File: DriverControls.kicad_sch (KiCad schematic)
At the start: 0 parts

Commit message: idk
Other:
- sheet LeaderSOM2 ports: added none; removed +12V_CarCAN, GND_CarCAN

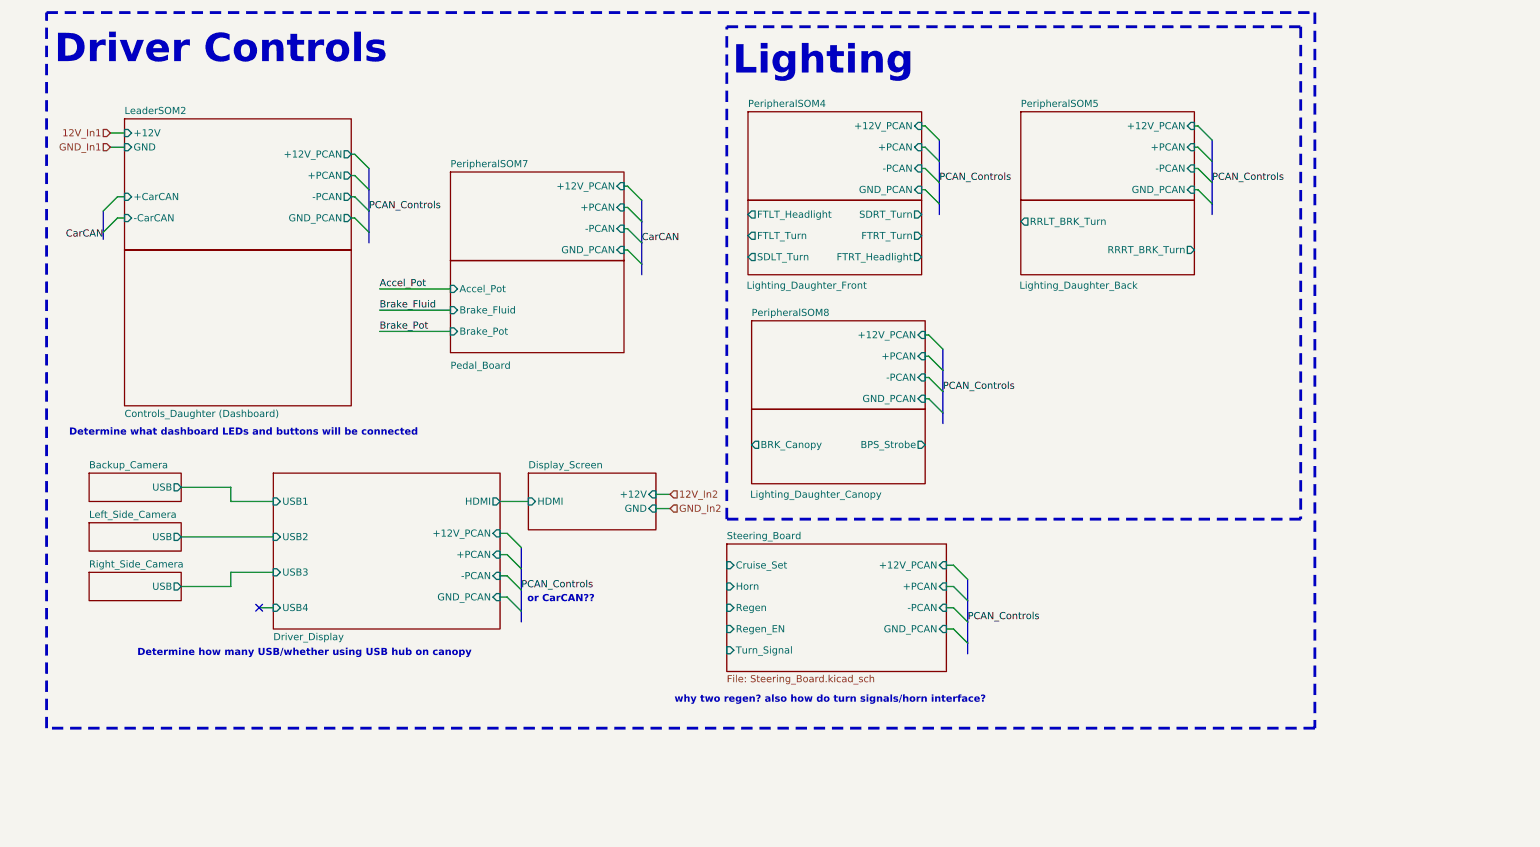
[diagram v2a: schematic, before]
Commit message: Updated Controls + Telemetry
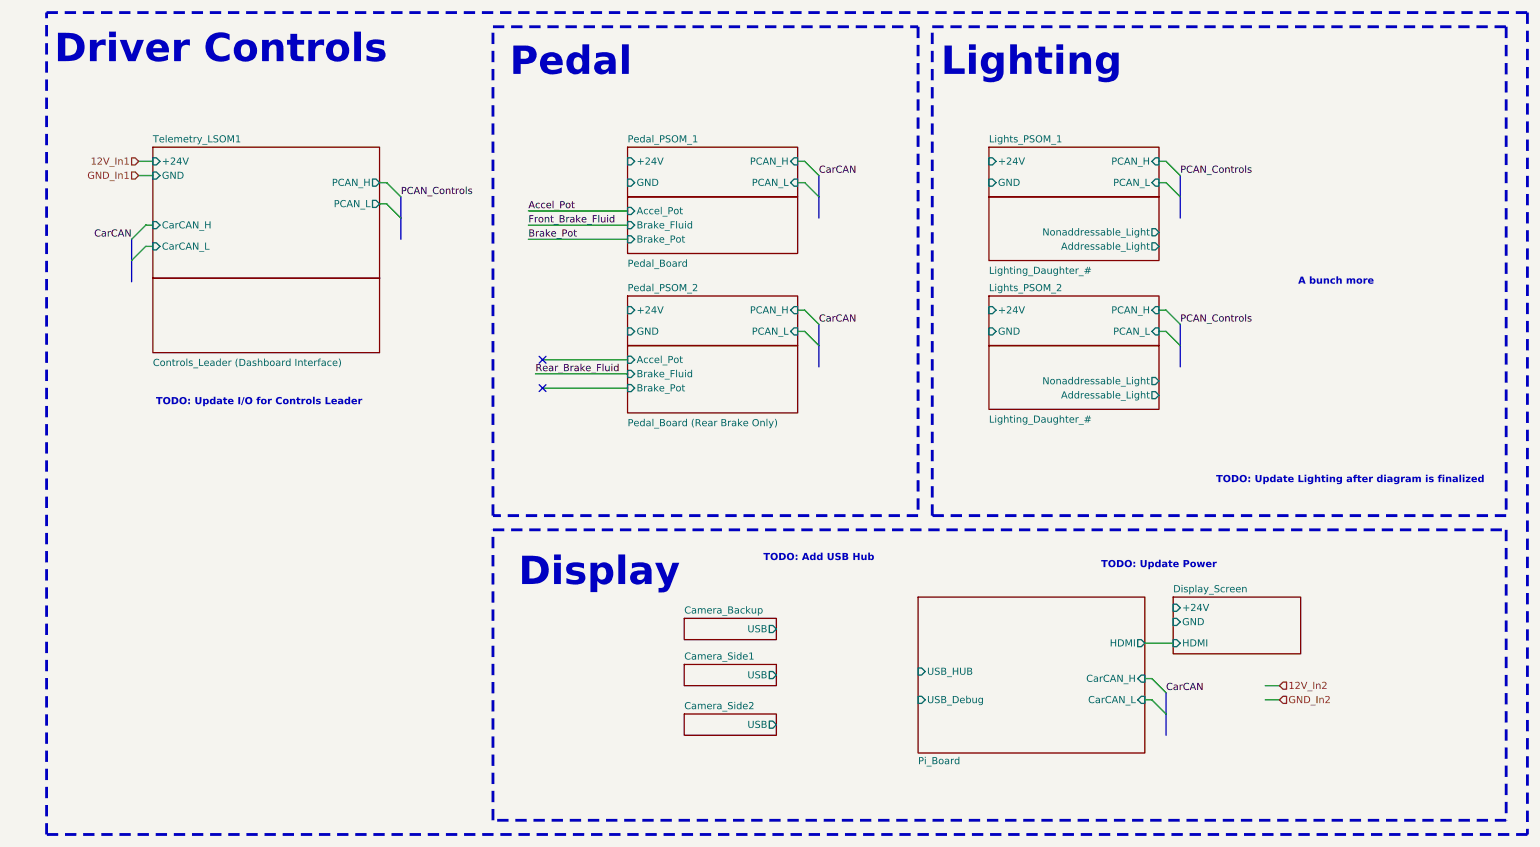
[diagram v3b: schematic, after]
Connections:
- no-connect marks 1 -> 2
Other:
- sheet Backup_Camera renamed Camera_Backup
- sheet Controls_Daughter (Dashboard) renamed Controls_Leader (Dashboard Interface)
- sheet Driver_Display renamed Pi_Board
- sheet Lighting_Daughter_Front renamed Lighting_Daughter_#
- sheet PeripheralSOM7 renamed Pedal_PSOM_1
- removed sheet LeaderSOM2
- removed sheet Left_Side_Camera
- removed sheet Lighting_Daughter_Back
- removed sheet Lighting_Daughter_Canopy
- removed sheet PeripheralSOM4
- removed sheet PeripheralSOM5
- removed sheet PeripheralSOM8
- removed sheet Right_Side_Camera
- removed sheet Steering_Board
- added sheet Camera_Side1 (Camera.kicad_sch)
- added sheet Camera_Side2 (Camera.kicad_sch)
- added sheet Lights_PSOM_1 (PeripheralSOM.kicad_sch)
- added sheet Lights_PSOM_2 (PeripheralSOM.kicad_sch)
- added sheet Pedal_Board (Rear Brake Only) (Pedal_Board.kicad_sch)
- added sheet Pedal_PSOM_2 (PeripheralSOM.kicad_sch)
- added sheet Telemetry_LSOM1 (LeaderSOM.kicad_sch)
- sheet Camera_Backup: file Backup_Camera.kicad_sch -> Camera.kicad_sch
- sheet Display_Screen ports: added +24V; removed +12V
- sheet Lighting_Daughter_# ports: added Addressable_Light, Nonaddressable_Light; removed FTLT_Headlight, FTLT_Turn, FTRT_Headlight, FTRT_Turn, SDLT_Turn, SDRT_Turn
- sheet Pedal_PSOM_1 ports: added +24V, GND, PCAN_H, PCAN_L; removed +12V_PCAN, +PCAN, -PCAN, GND_PCAN
- sheet Pi_Board ports: added CarCAN_H, CarCAN_L, USB_Debug, USB_HUB; removed +12V_PCAN, +PCAN, -PCAN, GND_PCAN, USB1, USB2, USB3, USB4
- note added: "A bunch more"
- note added: "Display"
- note added: "Pedal"
- note added: "TODO: Add USB Hub"
- note added: "TODO: Update I/O for Controls Leader"
- note added: "TODO: Update Lighting after diagram is finalized"
- note added: "TODO: Update Power"
- note removed: "Determine how many USB/whether using USB hub on canopy"
- note removed: "Determine what dashboard LEDs and buttons will be connected"
- note removed: "or CarCAN??"
- note removed: "why two regen? also how do turn signals/horn interface?"
